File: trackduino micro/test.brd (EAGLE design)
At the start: 48.1 x 21.9 mm, 28 parts, among them IC2 74AHC1G125DBV, SW1 SPST_TACT-KMR2, U1 ATMEGA168MLF, Y1 16MHZ

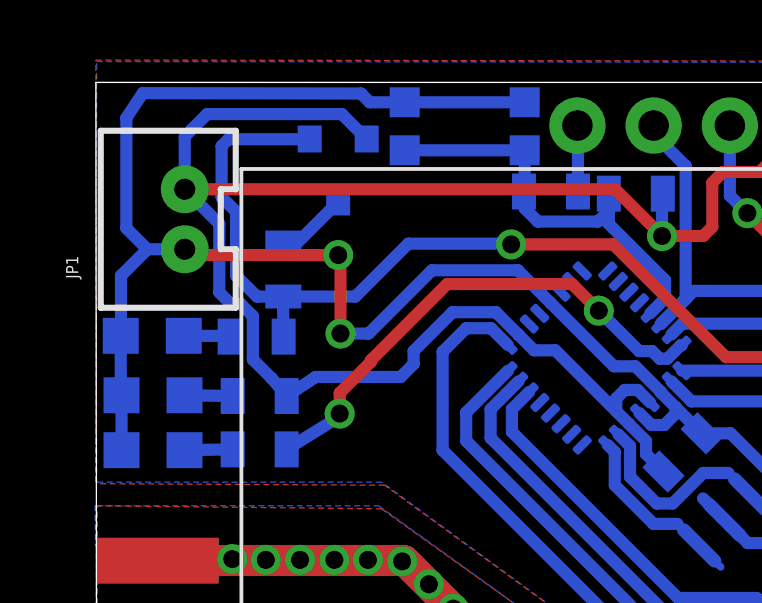
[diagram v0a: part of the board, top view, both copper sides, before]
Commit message: fixed consistency error on last commit
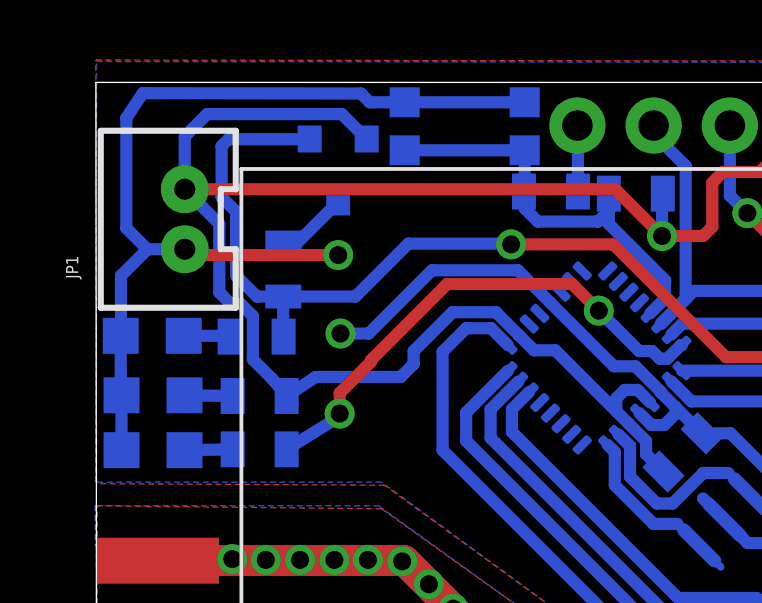
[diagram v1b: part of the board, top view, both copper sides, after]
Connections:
- new net S$1: C2.1, U$3.3
- net GND: no longer C2.1, U$3.3
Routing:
- net GND: track 157.3 -> 150.3 mm
- net S$1: track 0.00 -> 2.41 mm
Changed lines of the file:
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@@
 </elements>
 <signals>
+<signal name="S$1">
+<contactref element="C2" pad="1"/>
+<contactref element="U$3" pad="3"/>
+<wire x1="53.308" y1="73.925" x2="52.8828" y2="73.9758" width="0.4064" layer="16"/>
+<wire x1="53.308" y1="73.925" x2="54.7116" y2="75.3286" width="0.4064" layer="16"/>
+</signal>
 <signal name="GND">
 <contactref element="IC2" pad="3"/>
@@
 <via x="92.9386" y="67.6402" extent="1-16" drill="0.6" shape="square"/>
 <wire x1="92.9386" y1="67.6402" x2="92.9386" y2="69.0262" width="0.4064" layer="1"/>
-<contactref element="C2" pad="1"/>
-<contactref element="U$3" pad="3"/>
-<wire x1="53.308" y1="73.925" x2="52.8828" y2="73.9758" width="0.4064" layer="16"/>
-<wire x1="53.308" y1="73.925" x2="54.7116" y2="75.3286" width="0.4064" layer="16"/>
-<wire x1="54.7878" y1="70.9422" x2="54.7878" y2="73.4822" width="0.4064" layer="1"/>
-<wire x1="54.7878" y1="73.4822" x2="54.7116" y2="73.5584" width="0.4064" layer="1"/>
-<wire x1="54.7116" y1="73.5584" x2="53.3002" y2="73.5584" width="0.4064" layer="16"/>
-<wire x1="53.3002" y1="73.5584" x2="52.8828" y2="73.9758" width="0.4064" layer="16"/>
 <wire x1="47.4894" y1="67.056" x2="48.6918" y2="63.373" width="0" layer="19" extent="1-16"/>
 </signal>
